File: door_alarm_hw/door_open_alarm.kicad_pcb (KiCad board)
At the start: 2 copper layers, 57.4 x 48.1 mm, 60 parts, among them Q1 CJ2301 S1, Q2 BSS138PW,115, Q3 CJ2301 S1, SW3 SS-12D10L5, U1 ESP32-S3-MINI-1, U2 AP2114HA-3.3TRG1

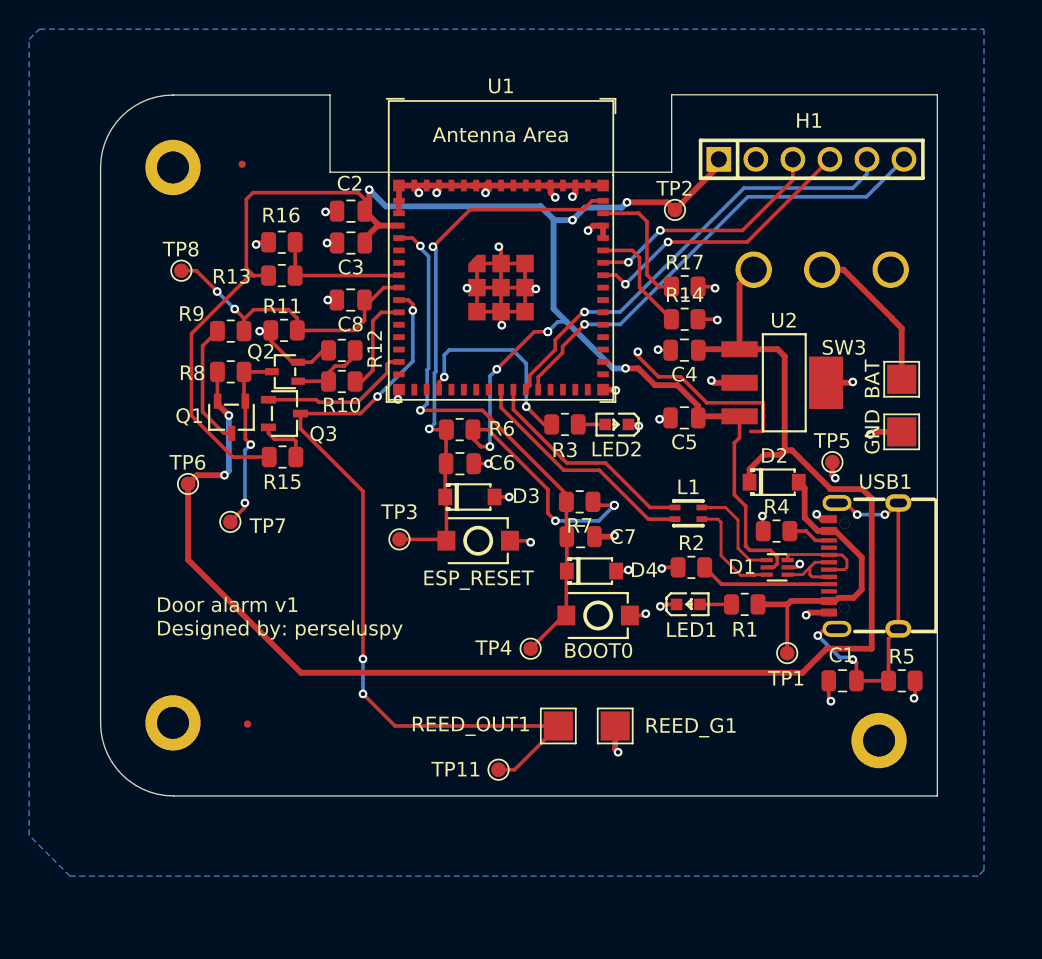
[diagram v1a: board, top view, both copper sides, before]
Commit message: Updating components and design as well as yaml
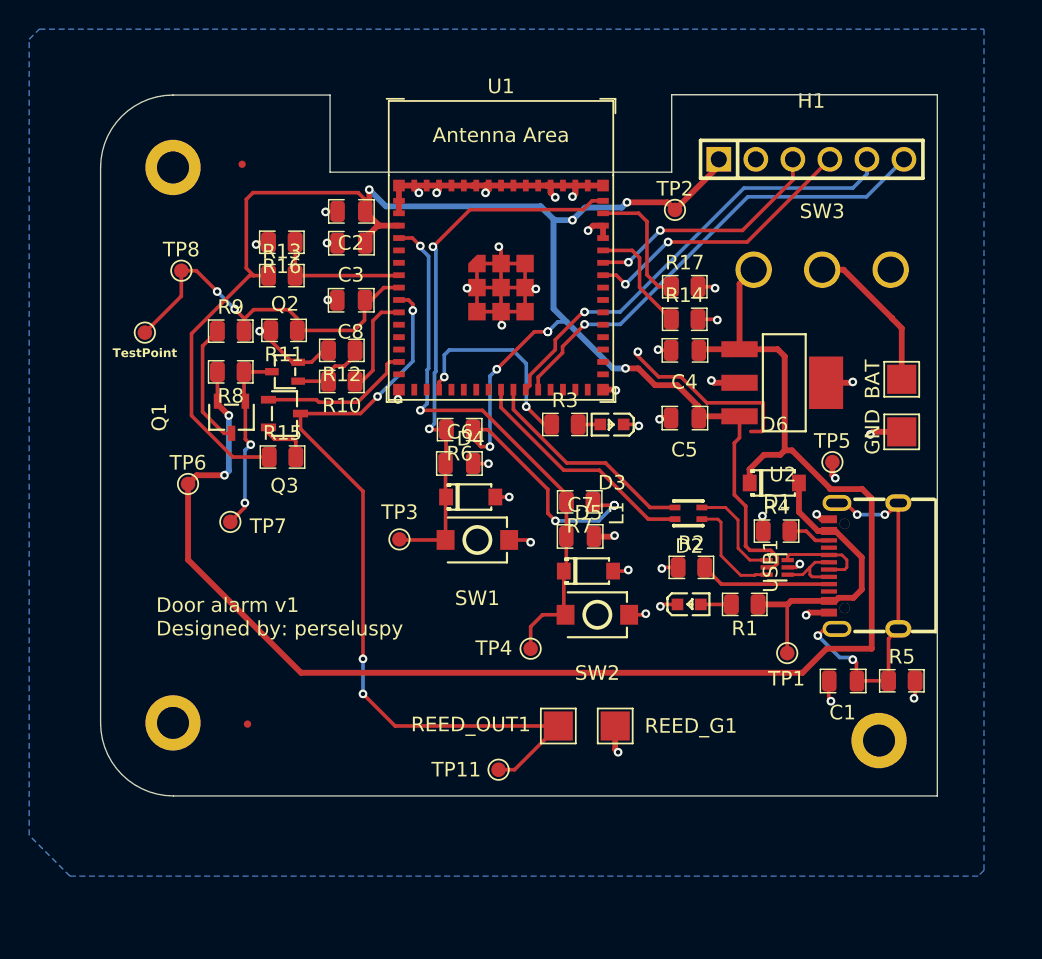
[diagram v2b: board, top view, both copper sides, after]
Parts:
- removed BOOT0, ESP_RESET: TS-1088-AR02016, my_lib:[TACTILE_SWITCH]XUNPU TS-1088-AR02016
- removed LED1, LED2: LTST-C190KRKT, my_lib:[LED]Lite-On LTST-C190KRKT
- added D5: STPS140Z, pepy_sym_lib:[SCHOTTKY_DIODE_40V]STMicroelectronics STPS140Z, F.Cu at (115.4, 96.8)
- added D6: STPS140Z, pepy_sym_lib:[SCHOTTKY_DIODE_40V]STMicroelectronics STPS140Z, F.Cu at (128.1, 90.7)
- added SW1: TS-1088-AR02016, pepy_sym_lib:[TACTILE_SWITCH]XUNPU TS-1088-AR02016, F.Cu at (107.7, 94.6)
- added SW2: TS-1088-AR02016, pepy_sym_lib:[TACTILE_SWITCH]XUNPU TS-1088-AR02016, F.Cu at (116.0, 99.8)
- added TP12: TestPoint, pepy_sym_lib:[TEST_POINT]TestPoint_Pad_D1.0mm, F.Cu at (84.9, 80.4)
- C1, C2, C3, C4, C5, C6, C7, C8: footprint Capacitor_SMD:C_0805_2012Metric -> pepy_sym_lib:[CAP_SMD]0805_2012Metric
- D1: footprint my_lib:SOT-666-6_L1.6-W1.2-P0.50-LS1.6-BR -> pepy_sym_lib:[ESD_PROT]STMicroelectronics USBLC6-2P6
- D2, D3: value STPS140Z -> LTST-C190KRKT; footprint my_lib:SOD-123_L2.8-W1.8-LS3.7-RD -> pepy_sym_lib:[LED]Lite-On LTST-C190KRKT
- D4: footprint my_lib:SOD-123_L2.8-W1.8-LS3.7-RD -> pepy_sym_lib:[SCHOTTKY_DIODE_40V]STMicroelectronics STPS140Z
- FID1, FID3: value Fiducial -> (none)
- H1: footprint my_lib:[6P_HEADER_STR]XFCN PZ254V-11-06P -> pepy_sym_lib:[6P_HEADER_STR]XFCN PZ254V-11-06P
- L1: footprint my_lib:FILTER-SMD_4P-L2.0-W1.2-BL_DLW21H -> pepy_sym_lib:[COMMON_MODE_FILTER]Murata Electronics DLW21SN900SQ2L
- Q1, Q3: footprint my_lib:[PMOS]Jiangsu Changjing Electronics Technology Co., Ltd. CJ2301 S1 -> pepy_sym_lib:[PMOS]Jiangsu Changjing Electronics Technology Co., Ltd. CJ2301 S1
- Q2: footprint my_lib:[NMOS]Nexperia BSS138PW,115 -> pepy_sym_lib:[NMOS]Nexperia BSS138PW,115
- R1, R10, R11, R12, R13, R14, R15, R16, R17, R2, R3, R4, R5, R6, R7, R8, R9: footprint Resistor_SMD:R_0805_2012Metric -> pepy_sym_lib:[RES_SMD]0805_2012Metric
- SW3: footprint my_lib:[SLIDE_SWITCH]XKB Connection SS-12D10L5 -> pepy_sym_lib:[SLIDE_SWITCH]XKB Connection SS-12D10L5
- U1: footprint PCM_Espressif:ESP32-S3-MINI-1 -> pepy_sym_lib:[MCU]Espressif Systems ESP32-S3-MINI-1-N8
- U2: footprint my_lib:[LDO]Diodes Incorporated AP2114HA-3.3TRG1 -> pepy_sym_lib:[LDO]Diodes Incorporated AP2114HA-3.3TRG1
- USB1: footprint my_lib:USB-C-SMD_TYPE-C-6PIN-2MD-073 -> pepy_sym_lib:[USB_C_16P_RA_FEMALE]SHOU HAN TYPE-C 16PIN 2MD(073)
- moved D3 10.9 mm to (117.0, 86.7), turned to 180 degrees
- moved D2 10.2 mm to (122.3, 99.1)
- moved D4 9.72 mm to (107.3, 91.7)
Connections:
- D2 pad 1: /V_INPUT -> GND
- D2 pad 2: /VBUS -> Net-(D2-A)
- D3 pad 1: /ESP_RESET -> GND
- D3 pad 2: GND -> Net-(D3-A)
- D4 pad 1: /BOOT0 -> /ESP_RESET
- R1 pad 2: Net-(LED1-A) -> Net-(D2-A)
- R12 pad 1: Net-(Q2-G) -> GND
- R12 pad 2: GND -> Net-(Q2-G)
- R3 pad 2: Net-(LED2-A) -> Net-(D3-A)
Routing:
- net /V_SENSE: track 21.4 -> 26.7 mm
- net Net-(LED1-A): track 2.16 -> 0.00 mm
- net Net-(D2-A): track 0.00 -> 2.10 mm
- net Net-(LED2-A): track 1.84 -> 0.00 mm
- net Net-(D3-A): track 0.00 -> 1.51 mm
- net /BOOT0: track 37.6 -> 38.5 mm
- net GND: track 87.9 -> 88.7 mm

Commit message: Overhaul
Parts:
- removed BAT: VCC, TestPoint:TestPoint_Pad_2.0x2.0mm
- removed GND: GND, TestPoint:TestPoint_Pad_2.0x2.0mm
- removed TP12: TestPoint, pepy_sym_lib:[TEST_POINT]TestPoint_Pad_D1.0mm
- added TP10: GND, pepy_sym_lib:[TEST_POINT]TestPoint_Pad_2.0x2.0mm, F.Cu at (136.8, 87.0)
- added TP9: VCC, pepy_sym_lib:[TEST_POINT]TestPoint_Pad_2.0x2.0mm, F.Cu at (136.8, 82.9)
- D1: value USBLC6-2P6 -> IP4283CZ10-TBR,115; footprint pepy_sym_lib:[ESD_PROT]STMicroelectronics USBLC6-2P6 -> pepy_sym_lib:[ESD_PROT]Nexperia IP4283CZ10-TBR,115
- TP1, TP11, TP2, TP3, TP4, TP5, TP6, TP7, TP8: footprint TestPoint:TestPoint_Pad_D1.0mm -> pepy_sym_lib:[TEST_POINT]TestPoint_Pad_D1.0mm
- moved D5 12.4 mm to (105.9, 88.7), turned to 90 degrees
- moved SW2 12.1 mm to (105.2, 94.3), turned to 90 degrees
- moved SW1 9.72 mm to (99.4, 89.7), turned to -90 degrees
- moved D4 8.16 mm to (99.9, 95.2), turned to -90 degrees
- moved R7 7.24 mm to (107.9, 89.6), turned to -90 degrees
- moved C7 6.99 mm to (107.9, 93.3), turned to -90 degrees
- moved C6 6.66 mm to (102.2, 94.5), turned to -90 degrees
- moved TP4 6.07 mm to (109.7, 96.3)
- moved R6 5.81 mm to (102.2, 90.9), turned to -90 degrees
- moved L1 5.77 mm to (126.2, 97.0)
- moved TP3 4.80 mm to (97.6, 94.2), turned to -90 degrees
- moved R2 4.52 mm to (126.0, 99.3)
- moved D2 3.37 mm to (122.9, 102.4)
- moved R1 3.33 mm to (126.5, 102.4)
- moved R4 2.43 mm to (126.0, 93.2)
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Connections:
- D1 pad 1: /D- -> unconnected-(D1-TMDS_CH1--Pad1)
- D1 pad 2: GND -> /D-
- D1 pad 3: /D+ -> GND
- D1 pad 4: /USB_D+ -> /D+
- D1 pad 5: +3.3V -> unconnected-(D1-TMDS_CH2+-Pad5)
- D1 pad 6: /USB_D- -> unconnected-(D1-NC-Pad6)
- L1 pad 1: /USB_D- -> /D-
- L1 pad 2: /USB_D-_FIL -> /USB_D-
- L1 pad 3: /USB_D+_FIL -> /USB_D+
- L1 pad 4: /USB_D+ -> /D+
- U1 pad 23: /USB_D-_FIL -> /USB_D-
- U1 pad 24: /USB_D+_FIL -> /USB_D+
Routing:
- net +3.3V: track 132.5 -> 111.5 mm, vias 12 -> 9
- net /USB_D-_FIL: track 16.3 -> 0.00 mm
- net /USB_D+: track 7.08 -> 23.3 mm
- net /USB_D-: track 7.41 -> 23.3 mm
- net /USB_D+_FIL: track 15.2 -> 0.00 mm
- net /ESP_RESET: track 38.0 -> 45.1 mm
- net /V_SENSE: track 26.7 -> 21.4 mm
- net /BOOT0: track 38.5 -> 33.3 mm
- net Net-(USB1-CC1): track 9.00 -> 5.65 mm
- net Net-(USB1-CC2): track 2.95 -> 5.57 mm
- net /D-: track 5.06 -> 7.55 mm
- net /REED: track 54.8 -> 56.6 mm, vias 4 -> 5
- net /VBUS: track 20.7 -> 22.1 mm
- net GND: track 88.7 -> 87.5 mm
- net VCC: track 10.6 -> 11.5 mm
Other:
- board text added: "Door alarm v2 perseluspy"
- board text removed: "Door alarm v1 Designed by: perseluspy"

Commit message: change++
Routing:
- net (no net): track 13.2 -> 0.00 mm, vias 1 -> 0
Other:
- board text added: "0"
- board text added: "0 mm"
- board text added: "0.01 mm"
- board text added: "0.02"
- board text added: "0.035 mm"
- board text added: "1"
- board text added: "1.51 mm"
- board text added: "3.3"
- board text added: "4.5"
- board text added: "B.Cu"
- board text added: "B.Mask"
- board text added: "B.Paste"
- board text added: "B.Silkscreen"
- board text added: "Bottom Silk Screen"
- board text added: "Bottom Solder Mask"
- board text added: "Bottom Solder Paste"
- board text added: "Color"
- board text added: "Dielectric"
- board text added: "Epsilon R"
- board text added: "F.Cu"
- board text added: "F.Mask"
- board text added: "F.Paste"
- board text added: "F.Silkscreen"
- board text added: "FR4"
- board text added: "Layer Name"
- board text added: "Loss Tangent"
- board text added: "Material"
- board text added: "Not specified"
- board text added: "Thickness (mm)"
- board text added: "Top Silk Screen"
- board text added: "Top Solder Mask"
- board text added: "Top Solder Paste"
- board text added: "Type"
- board text added: "copper"
- board text added: "core"

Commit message: Overhauling...
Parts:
- removed H2, H3, H4: MountingHole_Pad, MountingHole:MountingHole_2.2mm_M2_DIN965_Pad
- removed REED_G1: REED_G, TestPoint:TestPoint_Pad_2.0x2.0mm
- removed REED_OUT1: REED_OUT, TestPoint:TestPoint_Pad_2.0x2.0mm
- removed SW1, SW2: TS-1088-AR02016, pepy_sym_lib:[TACTILE_SWITCH]XUNPU TS-1088-AR02016
- removed SW3: SS-12D10L5, pepy_sym_lib:[SLIDE_SWITCH]XKB Connection SS-12D10L5
- removed USB1: TYPE-C 16PIN 2MD(073), pepy_sym_lib:[USB_C_16P_RA_FEMALE]SHOU HAN TYPE-C 16PIN 2MD(073)
- added F1: 0466.200NRHF, pepy_sym_lib:[FUSE_SMD_1206], F.Cu at (135.7, 81.4)
- added FID2: Fiducial, Fiducial:Fiducial_0.5mm_Mask1mm, F.Cu at (93.0, 67.4)
- added J1: TYPE-C 16PIN 2MD(073), pepy_sym_lib:[USB_C_16P_RA_FEMALE]SHOU HAN TYPE-C 16PIN 2MD(073), F.Cu at (134.4, 96.4)
- added MH1: ~, pepy_sym_lib:[MOUNTING_HOLE]MountingHole_2.2mm_M2_DIN965_Pad, F.Cu at (87.4, 69.1)
- added MH2: ~, pepy_sym_lib:[MOUNTING_HOLE]MountingHole_2.2mm_M2_DIN965_Pad, F.Cu at (87.4, 103.8)
- added S1: SS-12D10L5, pepy_sym_lib:[SLIDE_SWITCH]XKB Connection SS-12D10L5, F.Cu at (131.4, 76.2)
- added S2: TS-1088-AR02016, pepy_sym_lib:[TACTILE_SWITCH]XUNPU TS-1088-AR02016, F.Cu at (99.1, 97.5)
- added S3: TS-1088-AR02016, pepy_sym_lib:[TACTILE_SWITCH]XUNPU TS-1088-AR02016, F.Cu at (106.2, 95.5)
- C1, C7: value 1u -> CL21A106KOQNNNE; footprint pepy_sym_lib:[CAP_SMD]0805_2012Metric -> pepy_sym_lib:[CAP_SMD_0805_2012Metric]
- C2: value 10u -> CC0805KRX7R9BB104; footprint pepy_sym_lib:[CAP_SMD]0805_2012Metric -> pepy_sym_lib:[CAP_SMD_0805_2012Metric]
- C3: value 0.1u -> CL21A106KOQNNNE; footprint pepy_sym_lib:[CAP_SMD]0805_2012Metric -> pepy_sym_lib:[CAP_SMD_0805_2012Metric]
- C4, C5: value 22u -> C0805C105M4VACTU; footprint pepy_sym_lib:[CAP_SMD]0805_2012Metric -> pepy_sym_lib:[CAP_SMD_0805_2012Metric]
- C6: value 1u -> C0805C105M4VACTU; footprint pepy_sym_lib:[CAP_SMD]0805_2012Metric -> pepy_sym_lib:[CAP_SMD_0805_2012Metric]
- C8: value 1u -> CC0805KRX7R9BB104; footprint pepy_sym_lib:[CAP_SMD]0805_2012Metric -> pepy_sym_lib:[CAP_SMD_0805_2012Metric]
- D1: value IP4283CZ10-TBR,115 -> STPS140Z; footprint pepy_sym_lib:[ESD_PROT]Nexperia IP4283CZ10-TBR,115 -> pepy_sym_lib:[SCHOTTKY_DIODE_40V]STMicroelectronics STPS140Z
- D2: value LTST-C190KRKT -> STPS140Z; footprint pepy_sym_lib:[LED]Lite-On LTST-C190KRKT -> pepy_sym_lib:[SCHOTTKY_DIODE_40V]STMicroelectronics STPS140Z
- D3: value LTST-C190KRKT -> IP4283CZ10-TBR,115; footprint pepy_sym_lib:[LED]Lite-On LTST-C190KRKT -> pepy_sym_lib:[ESD_PROT]Nexperia IP4283CZ10-TBR,115
- D5, D6: value STPS140Z -> LTST-C190KRKT; footprint pepy_sym_lib:[SCHOTTKY_DIODE_40V]STMicroelectronics STPS140Z -> pepy_sym_lib:[LED]Lite-On LTST-C190KRKT
- FID1, FID3: value (none) -> Fiducial
- Q1: value CJ2301 S1 -> BSS138PW,115; footprint pepy_sym_lib:[PMOS]Jiangsu Changjing Electronics Technology Co., Ltd. CJ2301 S1 -> pepy_sym_lib:[NMOS]Nexperia BSS138PW,115
- Q2: value BSS138PW,115 -> CJ2301 S1; footprint pepy_sym_lib:[NMOS]Nexperia BSS138PW,115 -> pepy_sym_lib:[PMOS]Jiangsu Changjing Electronics Technology Co., Ltd. CJ2301 S1
- R1: value 470R -> 0805W8F1002T5E; footprint pepy_sym_lib:[RES_SMD]0805_2012Metric -> pepy_sym_lib:[RES_SMD_0805_2012Metric]
- R10: value 1k -> 0805W8F1002T5E; footprint pepy_sym_lib:[RES_SMD]0805_2012Metric -> pepy_sym_lib:[RES_SMD_0805_2012Metric]
- R11: value 15k 1% -> 0805W8F1003T5E; footprint pepy_sym_lib:[RES_SMD]0805_2012Metric -> pepy_sym_lib:[RES_SMD_0805_2012Metric]
- R12, R7: value 10k -> 0805W8F1002T5E; footprint pepy_sym_lib:[RES_SMD]0805_2012Metric -> pepy_sym_lib:[RES_SMD_0805_2012Metric]
- R13: value 10k -> 0805W8F5101T5E; footprint pepy_sym_lib:[RES_SMD]0805_2012Metric -> pepy_sym_lib:[RES_SMD_0805_2012Metric]
- R14: value 10k -> 0805W8J0203T5E; footprint pepy_sym_lib:[RES_SMD]0805_2012Metric -> pepy_sym_lib:[RES_SMD_0805_2012Metric]
- R15: value 30k -> 0805W8F1002T5E; footprint pepy_sym_lib:[RES_SMD]0805_2012Metric -> pepy_sym_lib:[RES_SMD_0805_2012Metric]
- R16, R17: value 10k -> 0805W8F4700T5E; footprint pepy_sym_lib:[RES_SMD]0805_2012Metric -> pepy_sym_lib:[RES_SMD_0805_2012Metric]
- R2: value 5.1k -> 0805W8F1002T5E; footprint pepy_sym_lib:[RES_SMD]0805_2012Metric -> pepy_sym_lib:[RES_SMD_0805_2012Metric]
- R3: value 470R -> 0805W8F5101T5E; footprint pepy_sym_lib:[RES_SMD]0805_2012Metric -> pepy_sym_lib:[RES_SMD_0805_2012Metric]
- R4: value 5.1k -> 0805W8F5101T5E; footprint pepy_sym_lib:[RES_SMD]0805_2012Metric -> pepy_sym_lib:[RES_SMD_0805_2012Metric]
- R5: value 1M -> 0805W8F1002T5E; footprint pepy_sym_lib:[RES_SMD]0805_2012Metric -> pepy_sym_lib:[RES_SMD_0805_2012Metric]
- R6: value 10k -> 0805W8F1004T5E; footprint pepy_sym_lib:[RES_SMD]0805_2012Metric -> pepy_sym_lib:[RES_SMD_0805_2012Metric]
- R8: value 100k -> 0805W8F1001T5E; footprint pepy_sym_lib:[RES_SMD]0805_2012Metric -> pepy_sym_lib:[RES_SMD_0805_2012Metric]
- R9: value 15k 1% -> 0805W8F1002T5E; footprint pepy_sym_lib:[RES_SMD]0805_2012Metric -> pepy_sym_lib:[RES_SMD_0805_2012Metric]
- TP10: value GND -> V_SENSE; footprint pepy_sym_lib:[TEST_POINT]TestPoint_Pad_2.0x2.0mm -> pepy_sym_lib:[TEST_POINT]TestPoint_Pad_D1.0mm
- TP11: value REED -> BOOT
- TP2: value 3.3V -> VBAT; footprint pepy_sym_lib:[TEST_POINT]TestPoint_Pad_D1.0mm -> pepy_sym_lib:[TEST_POINT]TestPoint_Pad_2.0x2.0mm
- TP3: value ESP_RESET -> GND; footprint pepy_sym_lib:[TEST_POINT]TestPoint_Pad_D1.0mm -> pepy_sym_lib:[TEST_POINT]TestPoint_Pad_2.0x2.0mm
- TP4: value BOOT0 -> GND
- TP5: value GND -> 3.3V
- TP6: value V_INPUT -> GND
- TP7: value EN -> ESP_RESET
- TP8: value V_SENSE -> EN
- TP9: value VCC -> REED; footprint pepy_sym_lib:[TEST_POINT]TestPoint_Pad_2.0x2.0mm -> pepy_sym_lib:[TEST_POINT]TestPoint_Pad_D1.0mm
- U1: value ESP32-S3-MINI-1 -> AP2114HA-3.3TRG1; footprint pepy_sym_lib:[MCU]Espressif Systems ESP32-S3-MINI-1-N8 -> pepy_sym_lib:[LDO]Diodes Incorporated AP2114HA-3.3TRG1
- U2: value AP2114HA-3.3TRG1 -> ESP32-S3-MINI-1; footprint pepy_sym_lib:[LDO]Diodes Incorporated AP2114HA-3.3TRG1 -> pepy_sym_lib:[MCU]Espressif Systems ESP32-S3-MINI-1-N8
- moved TP10 49.2 mm to (88.5, 77.2)
- moved C2 46.6 mm to (132.8, 104.1)
- moved R1 42.4 mm to (94.9, 74.1)
- moved R16 41.9 mm to (126.2, 101.5), turned to 0 degrees
- moved R2 41.4 mm to (94.9, 72.0)
- moved TP3 39.8 mm to (137.0, 88.8), turned to 0 degrees
- moved FID3 38.9 mm to (96.1, 107.5)
- moved R6 36.9 mm to (136.7, 104.1), turned to 0 degrees
- moved TP9 36.5 mm to (111.0, 108.8)
- moved FID1 36.5 mm to (128.4, 108.2)
- moved TP6 32.0 mm to (114.3, 108.8)
- moved R5 28.9 mm to (122.0, 79.5), turned to 180 degrees
- moved D2 27.0 mm to (98.0, 91.8), turned to 90 degrees
- moved R14 26.8 mm to (95.3, 76.7)
- moved C1 25.2 mm to (121.9, 81.6)
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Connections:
- C1 pad 1: /SHIELD -> /V_INPUT
- C2 pad 1: +3.3V -> /SHIELD
- C4 pad 1: /V_INPUT -> GND
- C4 pad 2: GND -> /ESP_RESET
- C5 pad 1: +3.3V -> GND
- C5 pad 2: GND -> /BOOT0
- C6 pad 1: /ESP_RESET -> GND
- C6 pad 2: GND -> /V_SENSE
- C7 pad 1: /BOOT0 -> +3.3V
- C8 pad 1: /V_SENSE -> GND
- C8 pad 2: GND -> +3.3V
- D1 pad 1: unconnected-(D1-TMDS_CH1--Pad1) -> /V_INPUT
- D1 pad 2: /D- -> /VBUS
- D2 pad 1: GND -> /ESP_RESET
- D2 pad 2: Net-(D2-A) -> GND
- D3 pad 1: GND -> unconnected-(D3-TMDS_CH1--Pad1)
- D3 pad 2: Net-(D3-A) -> /D-
- D4 pad 1: /ESP_RESET -> /BOOT0
- D5 pad 1: /BOOT0 -> Net-(D5-A)
- D6 pad 1: /V_INPUT -> Net-(D6-A)
- D6 pad 2: /VBUS -> GND
- Q1 pad 1: /EN -> Net-(Q1-G)
- Q1 pad 2: /V_INPUT -> GND
- Q1 pad 3: Net-(Q1-D) -> /EN
- Q2 pad 1: Net-(Q2-G) -> /EN
- Q2 pad 2: GND -> /V_INPUT
- Q2 pad 3: /EN -> Net-(Q2-D)
- R1 pad 1: /VBUS -> /STRAP_3
- R1 pad 2: Net-(D2-A) -> +3.3V
- R10 pad 1: /MEAS_EN -> /ESP_RESET
- R10 pad 2: Net-(Q2-G) -> +3.3V
- R11 pad 1: /V_SENSE -> /EN
- R11 pad 2: GND -> /V_INPUT
- R12 pad 1: GND -> Net-(Q3-S)
- R12 pad 2: Net-(Q2-G) -> +3.3V
- R13 pad 1: +3.3V -> /V_SENSE
- R13 pad 2: /STRAP_3 -> Net-(Q2-D)
- R14 pad 1: /STRAP_45 -> GND
- R14 pad 2: GND -> /V_SENSE
- R15 pad 1: +3.3V -> /BOOT0
- R15 pad 2: Net-(Q3-S) -> +3.3V
- R16 pad 1: /STRAP_3 -> Net-(D5-A)
- R16 pad 2: GND -> /VBUS
- R17 pad 1: /STRAP_46 -> Net-(D6-A)
- R17 pad 2: GND -> /LED_EN
- R2 pad 2: Net-(USB1-CC1) -> /STRAP_3
- R3 pad 1: /LED_EN -> GND
- R3 pad 2: Net-(D3-A) -> Net-(J1-CC1)
- R5 pad 1: /SHIELD -> GND
- R5 pad 2: GND -> /STRAP_45
- R6 pad 1: +3.3V -> /SHIELD
- R6 pad 2: /ESP_RESET -> GND
- R7 pad 1: +3.3V -> GND
- R7 pad 2: /BOOT0 -> /STRAP_46
- R8 pad 1: /EN -> /MEAS_EN
- R8 pad 2: /V_INPUT -> Net-(Q1-G)
- R9 pad 1: Net-(Q1-D) -> GND
- R9 pad 2: /V_SENSE -> Net-(Q1-G)
- TP10 pad 1: GND -> /V_SENSE
- TP11 pad 1: /REED -> /BOOT0
- TP2 pad 1: +3.3V -> VCC
- TP3 pad 1: /ESP_RESET -> GND
- TP4 pad 1: /BOOT0 -> GND
- TP5 pad 1: GND -> +3.3V
- TP6 pad 1: /V_INPUT -> GND
- TP7 pad 1: /EN -> /ESP_RESET
- TP8 pad 1: /V_SENSE -> /EN
- TP9 pad 1: VCC -> /REED
- U1 pad 1: GND -> /V_INPUT
- U1 pad 4: /BOOT0 -> GND
- U2 pad 1: /V_INPUT -> GND
- U2 pad 4: GND -> /BOOT0
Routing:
- net /REED: track 56.6 -> 46.5 mm, vias 5 -> 2
- net Net-(Q1-G): track 0.00 -> 8.96 mm
- net Net-(Q1-D): track 8.55 -> 0.00 mm
- net VCC: track 11.5 -> 4.27 mm
- net Net-(F1-Pad2): track 0.00 -> 6.77 mm
- net Net-(J1-CC1): track 0.00 -> 5.65 mm
- net Net-(USB1-CC1): track 5.65 -> 0.00 mm
- net Net-(Q2-G): track 4.98 -> 0.00 mm
- net /REED_EN: track 10.5 -> 5.86 mm
- net /MEAS_EN: track 6.97 -> 3.38 mm
- net Net-(Q2-D): track 0.00 -> 3.46 mm
- net GND: track 87.5 -> 90.1 mm, vias 41 -> 44
- net /VBUS: track 22.1 -> 19.7 mm
- net /V_SENSE: track 21.4 -> 19.5 mm, vias 2 -> 0
- net /EN: track 13.0 -> 14.8 mm, vias 2 -> 0
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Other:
- board size 57.4 x 48.1 mm -> 57.7 x 48.1 mm

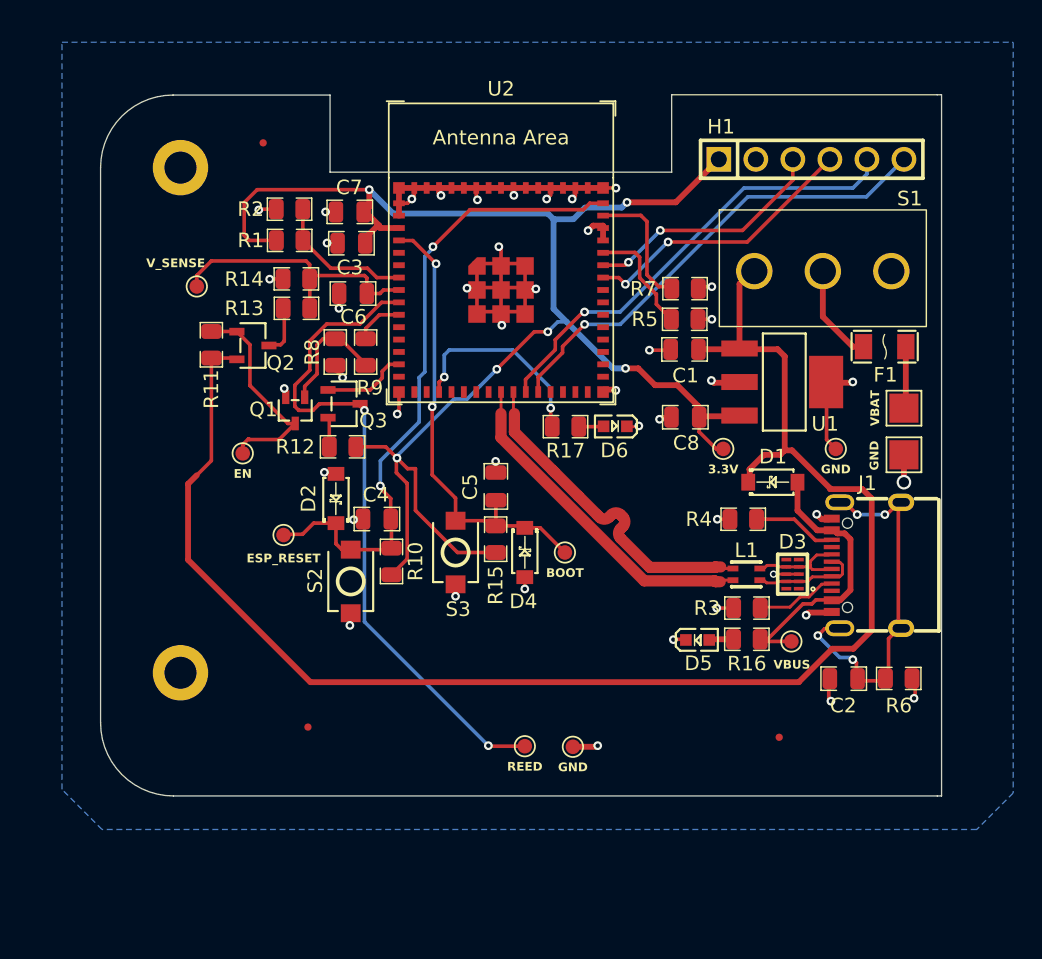
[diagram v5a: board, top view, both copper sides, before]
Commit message: Changes due to library update (minor)
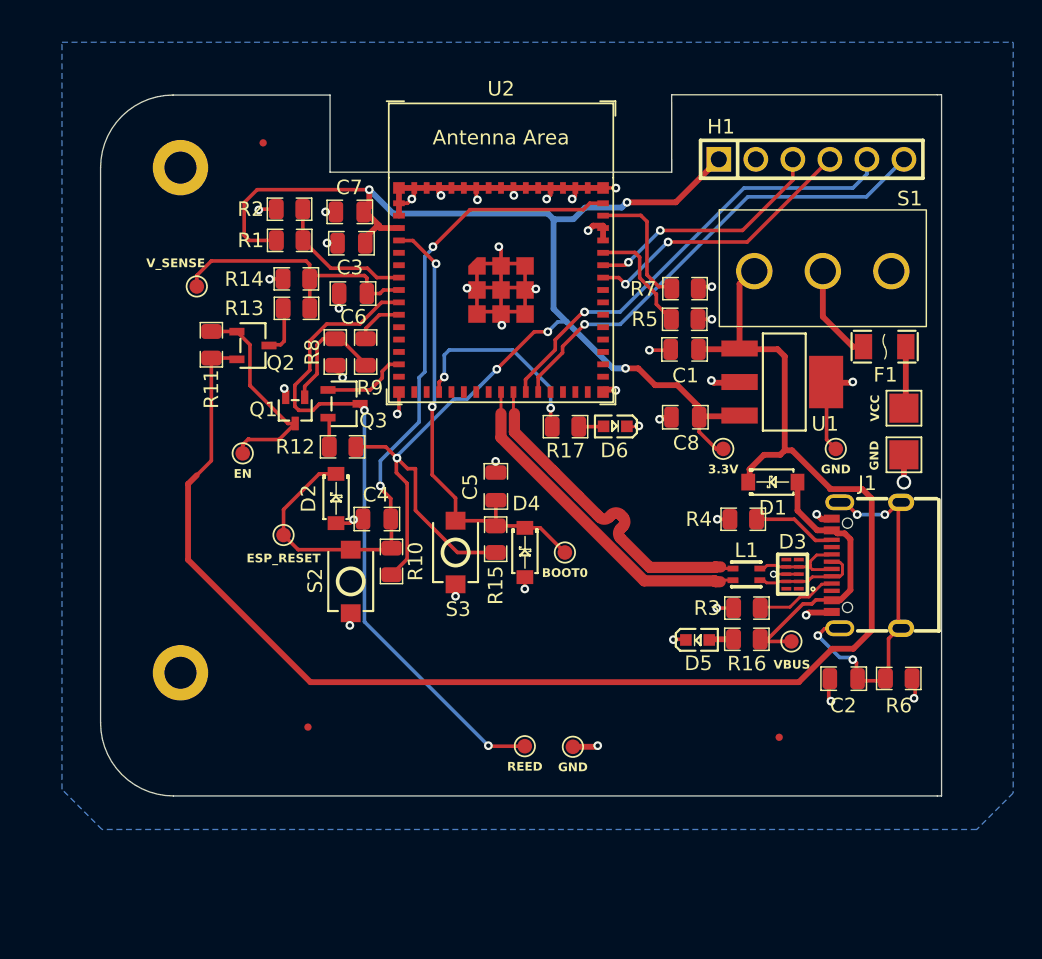
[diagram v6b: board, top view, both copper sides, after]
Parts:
- TP11: value BOOT -> BOOT0
- TP2: value VBAT -> VCC
- turned D1 to 180 degrees
- turned D4 to 90 degrees
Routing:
- net /ESP_RESET: track 44.5 -> 49.6 mm
- net GND: track 90.1 -> 90.6 mm, vias 44 -> 43
